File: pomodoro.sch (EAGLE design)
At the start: 26 parts, among them J1 POWER_JACK, J2 AVR_SPI_PROG_3X2PTH, U2 328P, Y1 16MHz

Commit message: Move parts a bit
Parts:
- R1, R2, R3, R4, R5, R6, R7, R8: value 10k -> 1k; device SparkFun-Resistors:10KOHM-HORIZ_KIT-1/4W-1% -> SparkFun-Resistors:1KOHM-HORIZ-1/4W-1%
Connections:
- removed net N$20: S1.1, U2.PC0(ADC0)
- new net N$1: R2.2, RED_LED.C
- net N$10: now also S1.1, U2.PB1(OC1A); no longer GREEN_LED.C, R8.2
- net N$4: now also GREEN_LED.C, R3.2; no longer D1.C, R2.2
- net N$5: now also D1.C, R4.2; no longer D2.C, R3.2
- net N$6: now also D2.C, R5.2; no longer D3.C, R4.2
- net N$7: now also D3.C, R6.2; no longer R7.2, RED_LED.C
- net N$8: now also R7.2; no longer R5.2
- net N$9: now also R8.2; no longer R6.2
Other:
- moved on the sheet: R2, R3, R4, R5, R6, R7, R8, S1

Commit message: Change layout
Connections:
- net N$18: now also U2.PB2(SS/OC1B); no longer U2.PD7(AIN1)
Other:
- moved on the sheet: LS1, S1
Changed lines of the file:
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@@
 <instance part="D5" gate="G$1" x="195.58" y="96.52"/>
 <instance part="GREEN_LED" gate="G$1" x="157.48" y="83.82"/>
-<instance part="LS1" gate="G$1" x="134.62" y="78.74" rot="R270"/>
-<instance part="S1" gate="G$1" x="134.62" y="45.72"/>
+<instance part="LS1" gate="G$1" x="129.54" y="66.04" rot="R270"/>
+<instance part="S1" gate="G$1" x="142.24" y="50.8"/>
 <instance part="RED_LED" gate="G$1" x="149.86" y="81.28"/>
-<instance part="GND7" gate="1" x="132.08" y="68.58"/>
+<instance part="GND7" gate="1" x="127" y="55.88"/>
 <instance part="GND8" gate="1" x="149.86" y="63.5"/>
 <instance part="GND9" gate="1" x="157.48" y="66.04"/>
@@
 <instance part="GND15" gate="1" x="27.94" y="139.7"/>
 <instance part="SUPPLY3" gate="G$1" x="55.88" y="160.02"/>
-<instance part="GND16" gate="1" x="144.78" y="43.18"/>
+<instance part="GND16" gate="1" x="147.32" y="43.18"/>
 <instance part="J2" gate="G$1" x="96.52" y="144.78"/>
 <instance part="SUPPLY4" gate="G$1" x="109.22" y="149.86"/>
@@
 <pinref part="LS1" gate="G$1" pin="2"/>
 <pinref part="GND7" gate="1" pin="GND"/>
-<wire x1="132.08" y1="76.2" x2="132.08" y2="71.12" width="0.1524" layer="91"/>
+<wire x1="127" y1="63.5" x2="127" y2="58.42" width="0.1524" layer="91"/>
 </segment>
 <segment>
@@
 <pinref part="S1" gate="G$1" pin="2"/>
 <pinref part="GND16" gate="1" pin="GND"/>
-<wire x1="139.7" y1="45.72" x2="144.78" y2="45.72" width="0.1524" layer="91"/>
+<wire x1="147.32" y1="50.8" x2="147.32" y2="45.72" width="0.1524" layer="91"/>
 </segment>
 <segment>
@@
 </segment>
 </net>
-<net name="N$18" class="0">
-<segment>
-<pinref part="U2" gate="G$1" pin="PD7(AIN1)"/>
-<pinref part="LS1" gate="G$1" pin="1"/>
-<wire x1="119.38" y1="81.28" x2="132.08" y2="81.28" width="0.1524" layer="91"/>
-<wire x1="132.08" y1="81.28" x2="132.08" y2="78.74" width="0.1524" layer="91"/>
-</segment>
-</net>
 <net name="N$19" class="0">
 <segment>
@@
 <pinref part="U2" gate="G$1" pin="PB1(OC1A)"/>
 <pinref part="S1" gate="G$1" pin="1"/>
-<wire x1="119.38" y1="73.66" x2="129.54" y2="73.66" width="0.1524" layer="91"/>
-<wire x1="129.54" y1="73.66" x2="129.54" y2="45.72" width="0.1524" layer="91"/>
-</segment>
-</net>
+<wire x1="119.38" y1="73.66" x2="137.16" y2="73.66" width="0.1524" layer="91"/>
+<wire x1="137.16" y1="73.66" x2="137.16" y2="50.8" width="0.1524" layer="91"/>
+</segment>
+</net>
+<net name="N$18" class="0">
+<segment>
+<pinref part="U2" gate="G$1" pin="PB2(SS/OC1B)"/>
+<pinref part="LS1" gate="G$1" pin="1"/>
+<wire x1="119.38" y1="71.12" x2="127" y2="71.12" width="0.1524" layer="91"/>
+<wire x1="127" y1="71.12" x2="127" y2="66.04" width="0.1524" layer="91"/>
+</segment>
+</net>

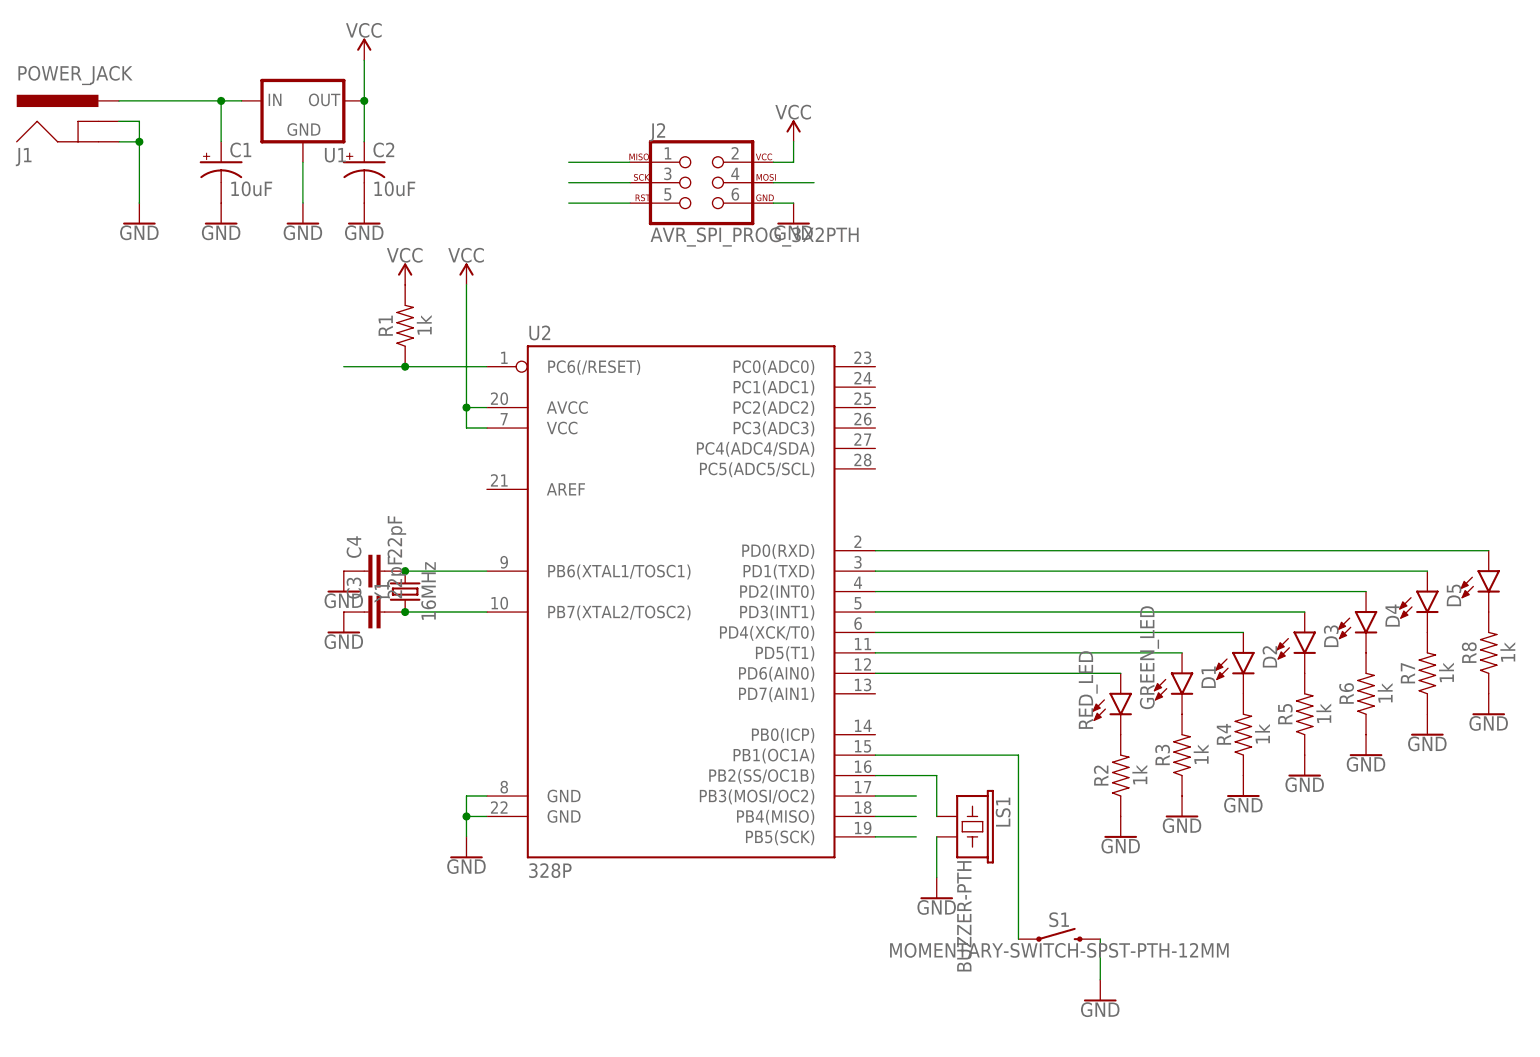
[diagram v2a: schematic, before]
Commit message: Change values of elements
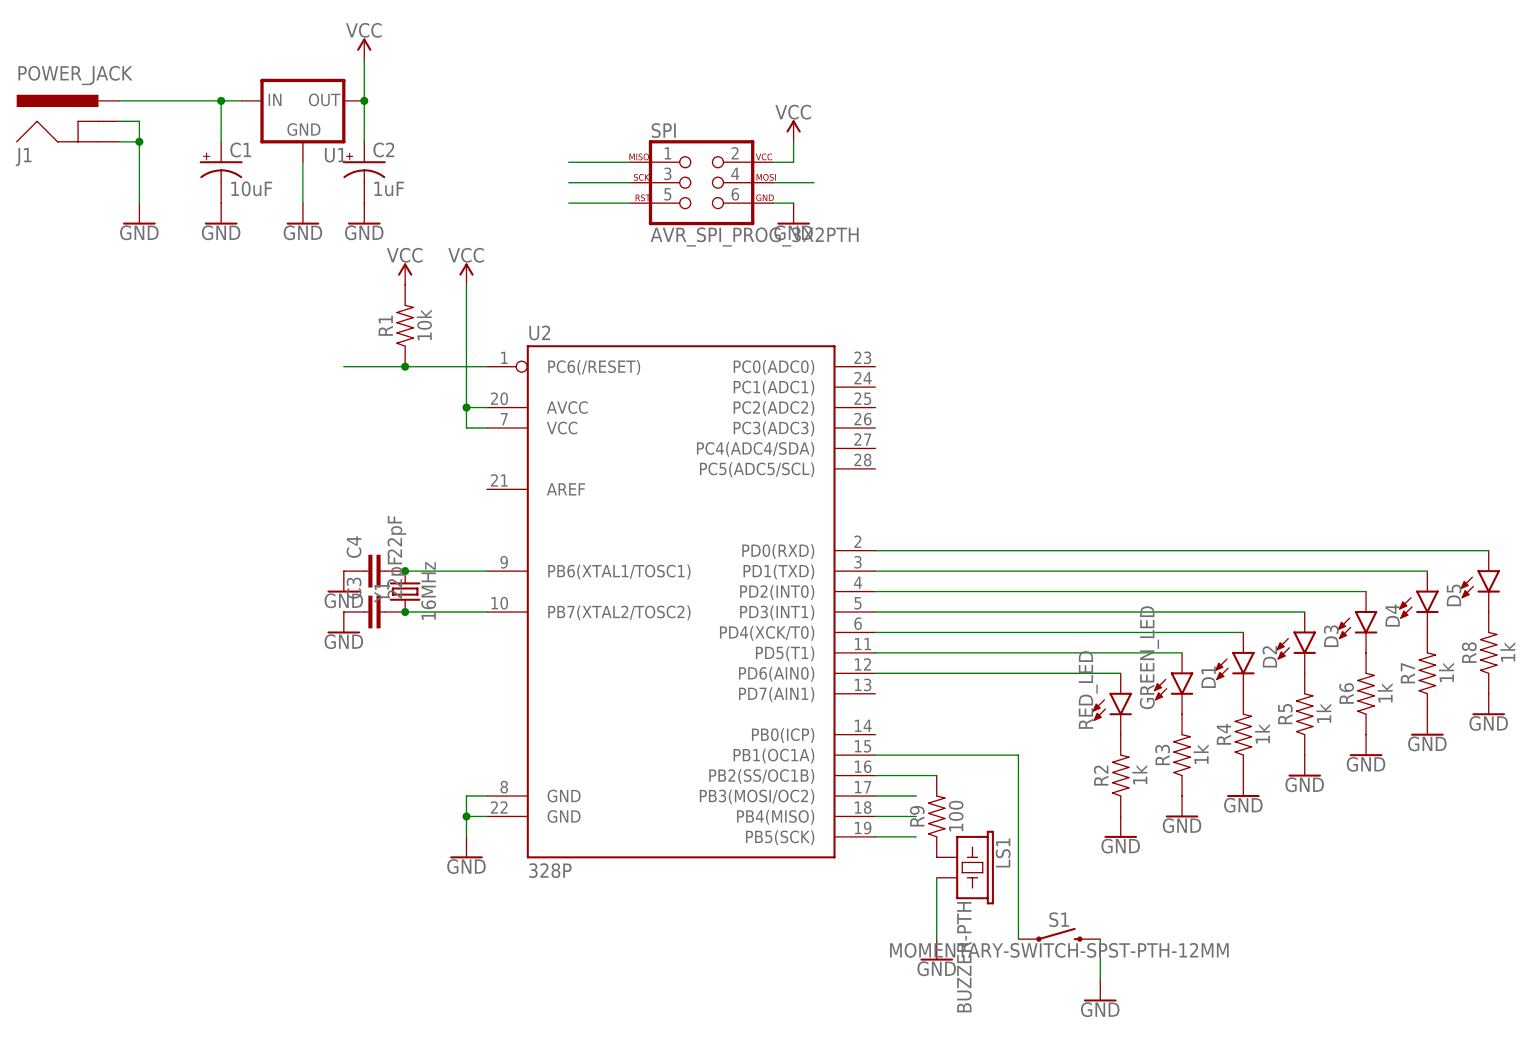
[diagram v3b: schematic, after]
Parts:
- added R9: 100, SparkFun-Resistors:1KOHM-HORIZ-1/4W-1%
- C2: value 10uF -> 1uF
- R1: value 1k -> 10k
- renumbered J2 to SPI
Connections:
- new net N$20: LS1.1, R9.1
- net N$18: now also R9.2; no longer LS1.1
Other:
- moved on the sheet: LS1
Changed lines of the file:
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@@
 <part name="U1" library="SparkFun-IC-Power" deviceset="V_REG_78XX" device="-TO-220"/>
 <part name="C1" library="SparkFun-Capacitors" deviceset="10UF-POLAR" device="-RADIAL-2.5MM-25V-20%" value="10uF"/>
-<part name="C2" library="SparkFun-Capacitors" deviceset="10UF-POLAR" device="-RADIAL-2.5MM-25V-20%" value="10uF"/>
+<part name="C2" library="SparkFun-Capacitors" deviceset="10UF-POLAR" device="-RADIAL-2.5MM-25V-20%" value="1uF"/>
 <part name="GND2" library="SparkFun-PowerSymbols" deviceset="GND" device=""/>
 <part name="GND3" library="SparkFun-PowerSymbols" deviceset="GND" device=""/>
@@
 <part name="SUPPLY3" library="SparkFun-PowerSymbols" deviceset="VCC" device=""/>
 <part name="GND16" library="SparkFun-PowerSymbols" deviceset="GND" device=""/>
-<part name="J2" library="SparkFun-Connectors" deviceset="AVR_SPI_PROG_3X2" device="PTH"/>
+<part name="SPI" library="SparkFun-Connectors" deviceset="AVR_SPI_PROG_3X2" device="PTH"/>
 <part name="SUPPLY4" library="SparkFun-PowerSymbols" deviceset="VCC" device=""/>
 <part name="GND17" library="SparkFun-PowerSymbols" deviceset="GND" device=""/>
@@
 <part name="R7" library="SparkFun-Resistors" deviceset="1KOHM" device="-HORIZ-1/4W-1%" value="1k"/>
 <part name="R8" library="SparkFun-Resistors" deviceset="1KOHM" device="-HORIZ-1/4W-1%" value="1k"/>
-<part name="R1" library="SparkFun-Resistors" deviceset="1KOHM" device="-HORIZ-1/4W-1%" value="1k"/>
+<part name="R1" library="SparkFun-Resistors" deviceset="1KOHM" device="-HORIZ-1/4W-1%" value="10k"/>
+<part name="R9" library="SparkFun-Resistors" deviceset="1KOHM" device="-HORIZ-1/4W-1%" value="100"/>
 </parts>
 <sheets>
@@
 <instance part="D5" gate="G$1" x="195.58" y="96.52"/>
 <instance part="GREEN_LED" gate="G$1" x="157.48" y="83.82"/>
-<instance part="LS1" gate="G$1" x="129.54" y="66.04" rot="R270"/>
+<instance part="LS1" gate="G$1" x="129.54" y="60.96" rot="R270"/>
 <instance part="S1" gate="G$1" x="142.24" y="50.8"/>
 <instance part="RED_LED" gate="G$1" x="149.86" y="81.28"/>
-<instance part="GND7" gate="1" x="127" y="55.88"/>
+<instance part="GND7" gate="1" x="127" y="48.26"/>
 <instance part="GND8" gate="1" x="149.86" y="63.5"/>
 <instance part="GND9" gate="1" x="157.48" y="66.04"/>
@@
 <instance part="SUPPLY3" gate="G$1" x="55.88" y="160.02"/>
 <instance part="GND16" gate="1" x="147.32" y="43.18"/>
-<instance part="J2" gate="G$1" x="96.52" y="144.78"/>
+<instance part="SPI" gate="G$1" x="96.52" y="144.78"/>
 <instance part="SUPPLY4" gate="G$1" x="109.22" y="149.86"/>
 <instance part="GND17" gate="1" x="109.22" y="139.7"/>
@@
 <instance part="R8" gate="G$1" x="195.58" y="86.36" rot="R90"/>
 <instance part="R1" gate="G$1" x="60.96" y="127" rot="R90"/>
+<instance part="R9" gate="G$1" x="127" y="66.04" rot="R90"/>
 </instances>
 <busses>
@@
 </segment>
 <segment>
-<pinref part="LS1" gate="G$1" pin="2"/>
-<pinref part="GND7" gate="1" pin="GND"/>
-<wire x1="127" y1="63.5" x2="127" y2="58.42" width="0.1524" layer="91"/>
-</segment>
-<segment>
 <pinref part="J1" gate="G$1" pin="GNDBREAK"/>
 <pinref part="GND15" gate="1" pin="GND"/>
@@
 </segment>
 <segment>
-<pinref part="J2" gate="G$1" pin="6"/>
+<pinref part="SPI" gate="G$1" pin="6"/>
 <pinref part="GND17" gate="1" pin="GND"/>
 <wire x1="106.68" y1="142.24" x2="109.22" y2="142.24" width="0.1524" layer="91"/>
@@
 <pinref part="GND14" gate="1" pin="GND"/>
 <pinref part="R8" gate="G$1" pin="1"/>
+</segment>
+<segment>
+<pinref part="LS1" gate="G$1" pin="2"/>
+<pinref part="GND7" gate="1" pin="GND"/>
+<wire x1="127" y1="58.42" x2="127" y2="50.8" width="0.1524" layer="91"/>
 </segment>
 </net>
@@
 <segment>
 <pinref part="SUPPLY4" gate="G$1" pin="VCC"/>
-<pinref part="J2" gate="G$1" pin="2"/>
+<pinref part="SPI" gate="G$1" pin="2"/>
 <wire x1="109.22" y1="149.86" x2="109.22" y2="147.32" width="0.1524" layer="91"/>
 <wire x1="109.22" y1="147.32" x2="106.68" y2="147.32" width="0.1524" layer="91"/>
@@
 <net name="MOSI" class="0">
 <segment>
-<pinref part="J2" gate="G$1" pin="4"/>
+<pinref part="SPI" gate="G$1" pin="4"/>
 <wire x1="106.68" y1="144.78" x2="111.76" y2="144.78" width="0.1524" layer="91"/>
 </segment>
@@
 <net name="RST" class="0">
 <segment>
-<pinref part="J2" gate="G$1" pin="5"/>
+<pinref part="SPI" gate="G$1" pin="5"/>
 <wire x1="88.9" y1="142.24" x2="81.28" y2="142.24" width="0.1524" layer="91"/>
 </segment>
@@
 <net name="SCK" class="0">
 <segment>
-<pinref part="J2" gate="G$1" pin="3"/>
+<pinref part="SPI" gate="G$1" pin="3"/>
 <wire x1="88.9" y1="144.78" x2="81.28" y2="144.78" width="0.1524" layer="91"/>
 </segment>
@@
 <net name="MISO" class="0">
 <segment>
-<pinref part="J2" gate="G$1" pin="1"/>
+<pinref part="SPI" gate="G$1" pin="1"/>
 <wire x1="88.9" y1="147.32" x2="81.28" y2="147.32" width="0.1524" layer="91"/>
 </segment>
@@
 <segment>
 <pinref part="U2" gate="G$1" pin="PB2(SS/OC1B)"/>
+<wire x1="119.38" y1="71.12" x2="127" y2="71.12" width="0.1524" layer="91"/>
+<pinref part="R9" gate="G$1" pin="2"/>
+</segment>
+</net>
+<net name="N$20" class="0">
+<segment>
+<pinref part="R9" gate="G$1" pin="1"/>
 <pinref part="LS1" gate="G$1" pin="1"/>
-<wire x1="119.38" y1="71.12" x2="127" y2="71.12" width="0.1524" layer="91"/>
-<wire x1="127" y1="71.12" x2="127" y2="66.04" width="0.1524" layer="91"/>
-</segment>
-</net>
+</segment>
+</net>
